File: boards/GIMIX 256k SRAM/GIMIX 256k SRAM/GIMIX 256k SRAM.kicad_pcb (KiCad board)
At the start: 2 copper layers, 247.7 x 140.3 mm, 110 parts, among them P1 SS-50 Bus, Q1 BC337, Q2 BC337, U1 HM62256BLP, U10 HM62256BLP, U11 HM62256BLP, U12 HM62256BLP, U13 HM62256BLP, U14 HM62256BLP, U15 HM62256BLP, U16 HM62256BLP, U17 HM62256BLP, U18 HM62256BLP, U19 HM62256BLP, U2 HM62256BLP, U20 HM62256BLP, U21 HM62256BLP, U22 HM62256BLP, U23 HM62256BLP, U24 HM62256BLP, U25 HM62256BLP, U26 HM62256BLP, U27 HM62256BLP, U28 HM62256BLP, U29 HM62256BLP, U3 HM62256BLP, U30 HM62256BLP, U31 HM62256BLP, U32 HM62256BLP, U33 74LS138, U34 74LS138, U35 74LS138, U36 74F244, U37 74LS138, U39 PAL16L8, U4 HM62256BLP, U40 74F244, U41 74F244, U42 74LS640, U46 LM7805_TO220, U47 LM7805_TO220, U48 LM7805_TO220, U49 74LS641, U5 HM62256BLP, U6 HM62256BLP, U7 HM62256BLP, U8 HM62256BLP, U9 HM62256BLP

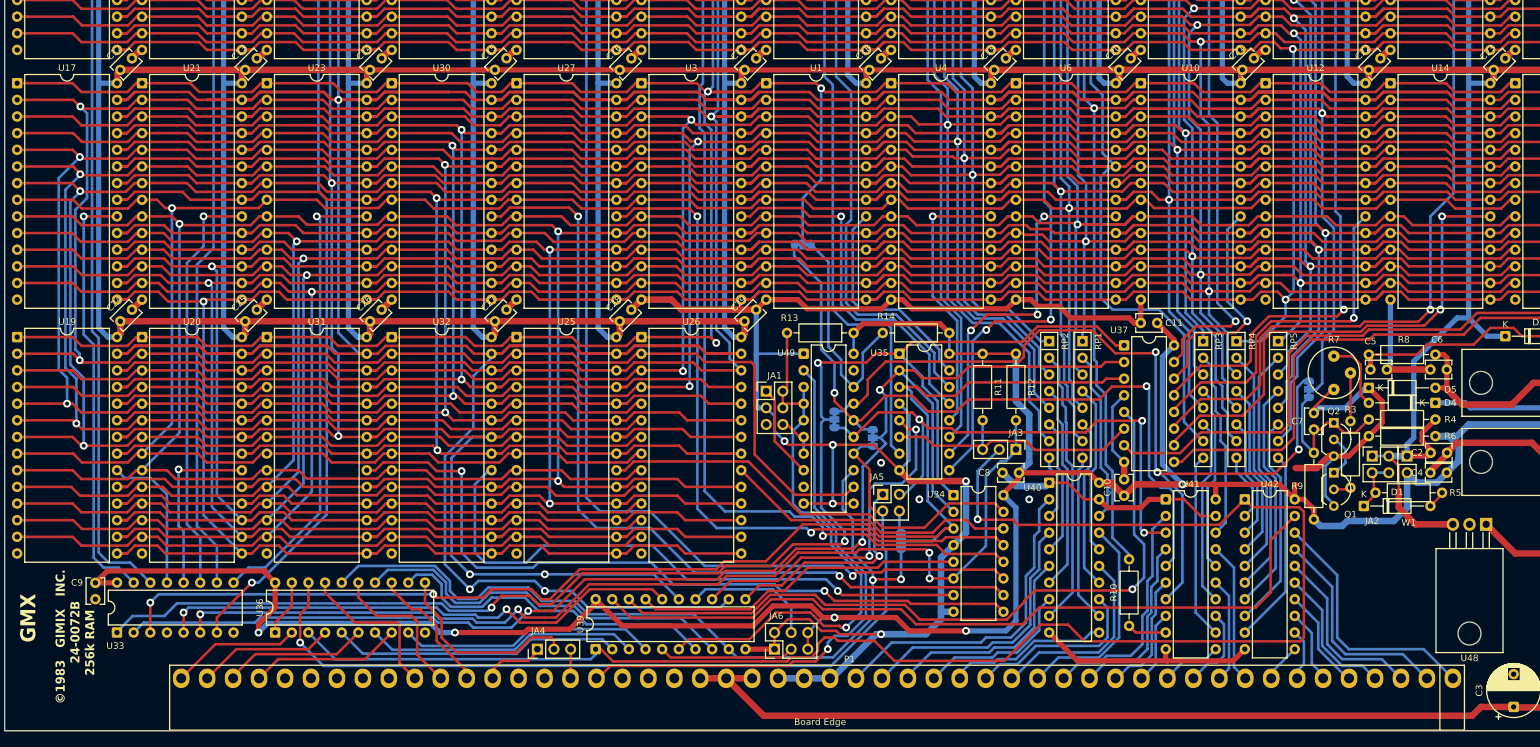
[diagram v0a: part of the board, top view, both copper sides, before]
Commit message: 256k RAM production version added
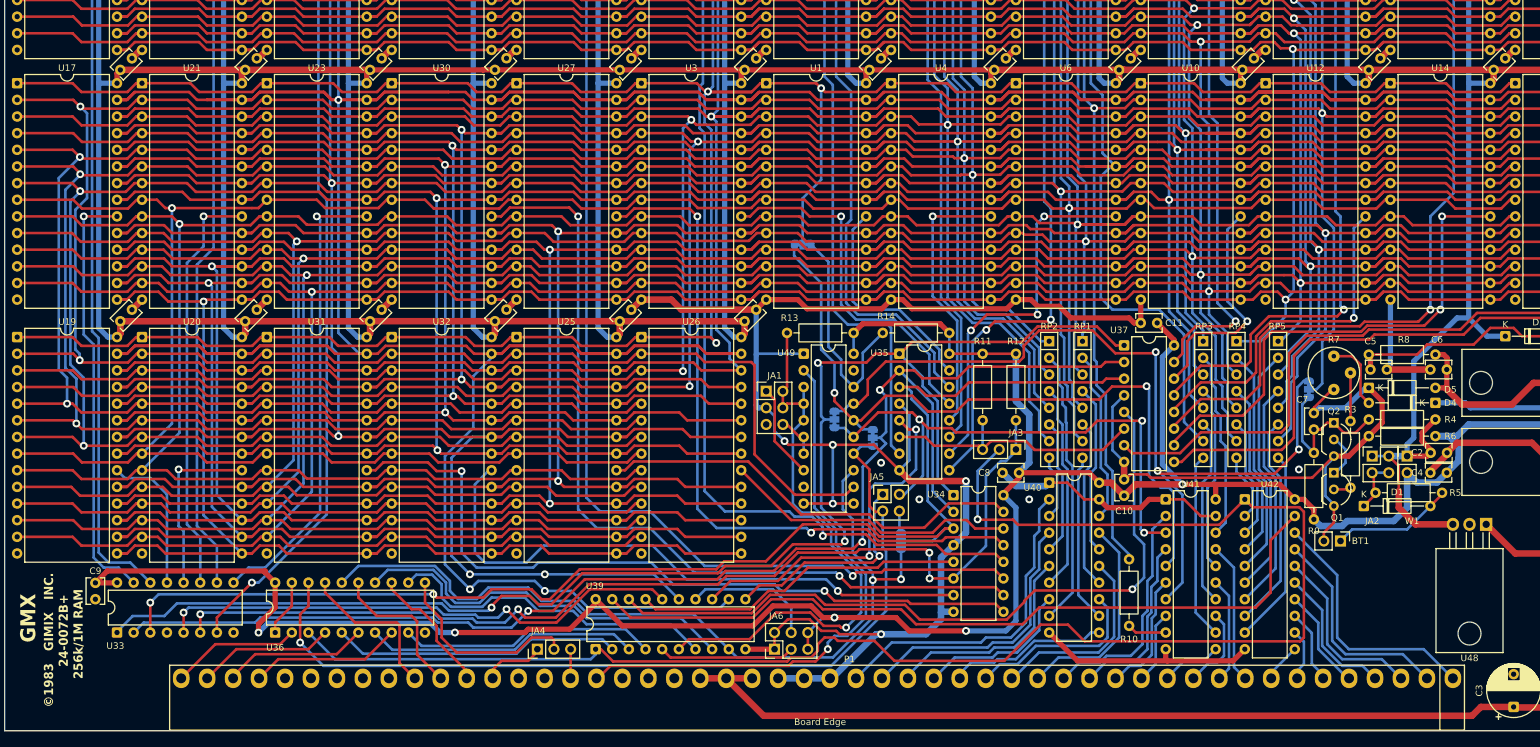
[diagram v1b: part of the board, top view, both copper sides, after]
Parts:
- added BT1: Battery, Connector_PinHeader_2.54mm:PinHeader_1x02_P2.54mm_Vertical, F.Cu at (224.8, 127.0)
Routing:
- net GND: track 472.1 -> 505.4 mm, vias 8 -> 9
- net Net-(BT1-+): track 2.77 -> 18.7 mm
- net +5V: track 395.4 -> 393.0 mm
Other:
- board text added: "©1983 GIMIX INC. 24-0072B+ 256k/1M RAM"
- board text removed: "©1983 GIMIX INC. 24-0072B 256k RAM"
